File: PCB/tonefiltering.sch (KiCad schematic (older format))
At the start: 14 parts, among them U10 TS4990IST, U9 TS4990IST

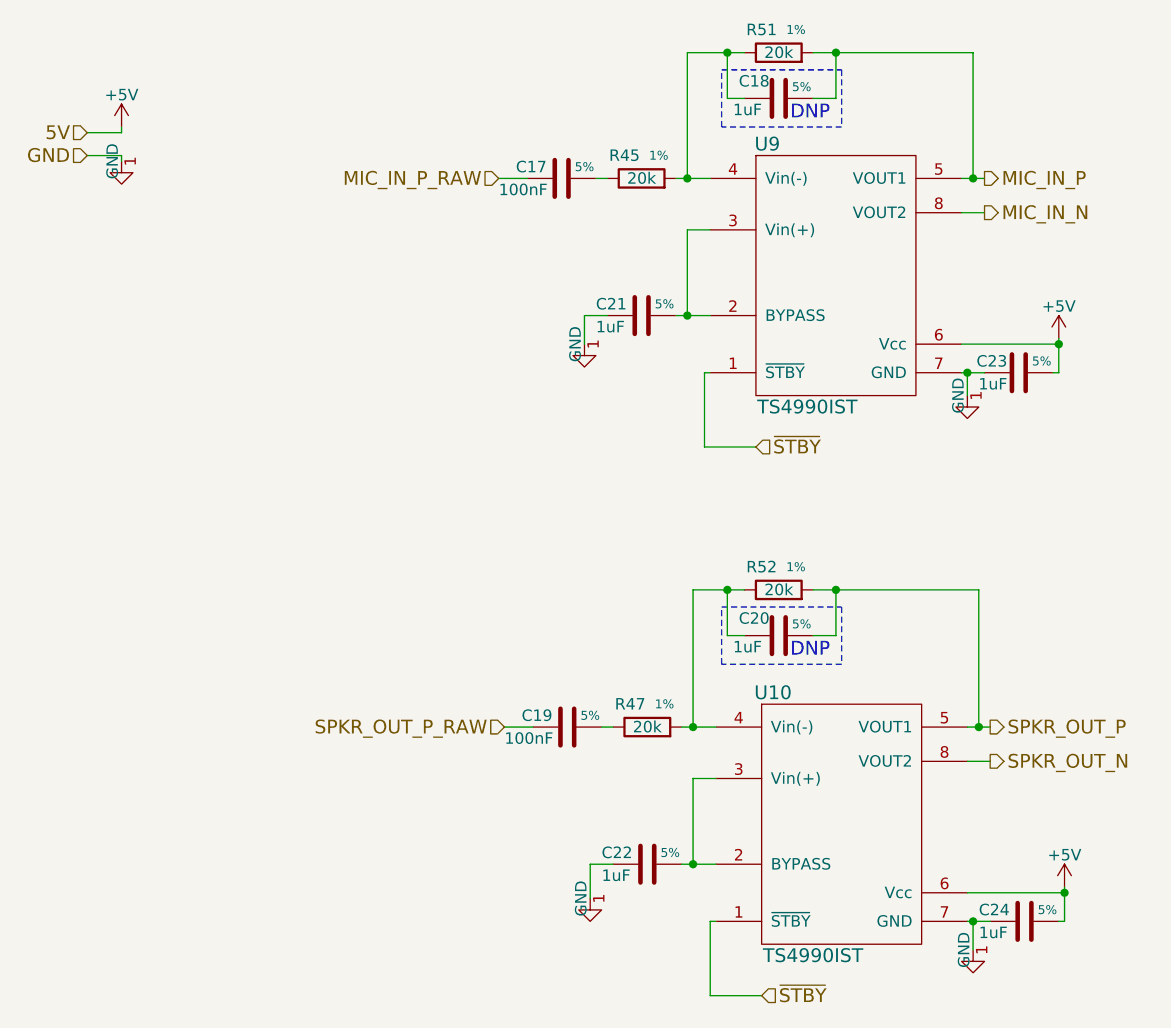
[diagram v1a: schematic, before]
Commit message: Added PCB layout
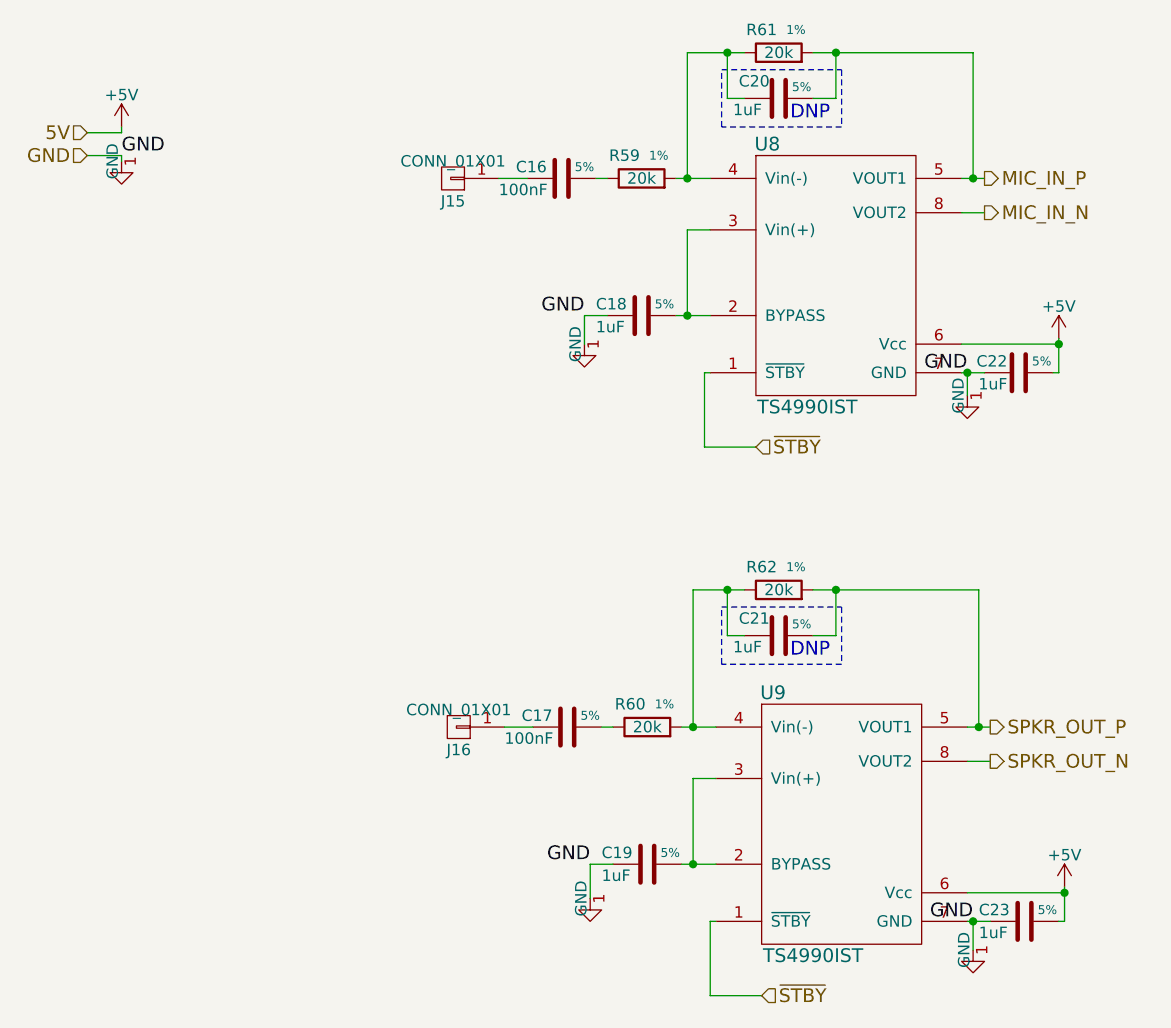
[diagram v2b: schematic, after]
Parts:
- added J15, J16: CONN_01X01, Pin_Headers:Pin_Header_Straight_1x01_Pitch2.54mm, symbol CONN_01X01
- C16: renamed from C17; footprint Footprints:1206 -> Capacitors_SMD:C_0603_HandSoldering
- C17: renamed from C19; footprint Footprints:1206 -> Capacitors_SMD:C_0603_HandSoldering
- C18: renamed from C21; footprint Footprints:1206 -> Capacitors_SMD:C_0603_HandSoldering
- C19: renamed from C22; footprint Footprints:1206 -> Capacitors_SMD:C_0603_HandSoldering
- C20: renamed from C18; footprint Footprints:1206 -> Capacitors_SMD:C_0603_HandSoldering
- C21: renamed from C20; footprint Footprints:1206 -> Capacitors_SMD:C_0603_HandSoldering
- C22: renamed from C23; footprint Footprints:1206 -> Capacitors_SMD:C_0603_HandSoldering
- C23: renamed from C24; footprint Footprints:1206 -> Capacitors_SMD:C_0603_HandSoldering
- R59: renamed from R45; footprint (none) -> Resistors_SMD:R_0603_HandSoldering
- R60: renamed from R47; footprint (none) -> Resistors_SMD:R_0603_HandSoldering
- R61: renamed from R51; footprint (none) -> Resistors_SMD:R_0603_HandSoldering
- R62: renamed from R52; footprint (none) -> Resistors_SMD:R_0603_HandSoldering
- U8: renamed from U9; footprint (none) -> Housings_SSOP:MSOP-8_3x3mm_Pitch0.65mm
- U9: renamed from U10; footprint (none) -> Housings_SSOP:MSOP-8_3x3mm_Pitch0.65mm
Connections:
- net GND: now also C18.2, C19.2, C22.1, C23.2, U8.7 (GND), U9.7 (GND)
- net MIC_IN_P_RAW: no longer names the net of C16.2
- net MIC_IN_P_RAW: now also J15.1 (P1)
- net SPKR_OUT_P_RAW: no longer names the net of C17.2
- net SPKR_OUT_P_RAW: now also J16.1 (P1)
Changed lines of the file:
@@
 $EndDescr
 $Comp
-L TS4990IST U9
+L TS4990IST U8
 U 1 1 5A23E919
 P 5200 2575
-F 0 "U9" H 5150 3025 60  0000 C CNN
+F 0 "U8" H 5150 3025 60  0000 C CNN
 F 1 "TS4990IST" H 5325 1875 60  0000 C CNN
-F 2 "" H 4500 3150 60  0001 C CNN
+F 2 "Housings_SSOP:MSOP-8_3x3mm_Pitch0.65mm" H 4500 3150 60  0001 C CNN
 F 3 "" H 4500 3150 60  0001 C CNN
 	1    5200 2575
@@
 $EndComp
 $Comp
-L C C17
+L C C16
 U 1 1 5A23E92A
 P 4250 2275
-F 0 "C17" V 4200 2075 50  0000 L CNN
+F 0 "C16" V 4200 2075 50  0000 L CNN
 F 1 "100nF" V 4300 2000 50  0000 L CNN
-F 2 "Footprints:1206" H 4288 2125 50  0001 C CNN
+F 2 "Capacitors_SMD:C_0603_HandSoldering" H 4288 2125 50  0001 C CNN
 F 3 "" H 4250 2275 50  0001 C CNN
 F 4 "5%" V 4200 2375 39  0000 C CNN "%"
@@
 	4400 2275 4450 2275
 $Comp
-L C C21
+L C C18
 U 1 1 5A23E93E
 P 4600 2875
-F 0 "C21" V 4550 2675 50  0000 L CNN
+F 0 "C18" V 4550 2675 50  0000 L CNN
 F 1 "1uF" V 4650 2675 50  0000 L CNN
-F 2 "Footprints:1206" H 4638 2725 50  0001 C CNN
+F 2 "Capacitors_SMD:C_0603_HandSoldering" H 4638 2725 50  0001 C CNN
 F 3 "" H 4600 2875 50  0001 C CNN
 F 4 "5%" V 4550 2975 39  0000 C CNN "%"
@@
 Connection ~ 4800 2875
 $Comp
-L C C23
+L C C22
 U 1 1 5A23E94C
 P 6250 3125
-F 0 "C23" V 6300 3175 50  0000 L CNN
+F 0 "C22" V 6300 3175 50  0000 L CNN
 F 1 "1uF" V 6200 3175 50  0000 L CNN
-F 2 "Footprints:1206" H 6288 2975 50  0001 C CNN
+F 2 "Capacitors_SMD:C_0603_HandSoldering" H 6288 2975 50  0001 C CNN
 F 3 "" H 6250 3125 50  0001 C CNN
 F 4 "5%" V 6300 3025 39  0000 C CNN "%"
@@
 	6000 2275 6100 2275
 $Comp
-L R R51
+L R R61
 U 1 1 5A23E96E
 P 5200 1725
-F 0 "R51" V 5300 1800 50  0000 C CNN
+F 0 "R61" V 5300 1800 50  0000 C CNN
 F 1 "20k" V 5200 1725 50  0000 C CNN
-F 2 "" V 5130 1725 50  0001 C CNN
+F 2 "Resistors_SMD:R_0603_HandSoldering" V 5130 1725 50  0001 C CNN
 F 3 "" H 5200 1725 50  0001 C CNN
 F 4 "1%" V 5300 1650 39  0000 C CNN "%"
@@
 Connection ~ 6050 2275
 $Comp
-L R R45
+L R R59
 U 1 1 5A23E97C
 P 4600 2275
-F 0 "R45" V 4700 2350 50  0000 C CNN
+F 0 "R59" V 4700 2350 50  0000 C CNN
 F 1 "20k" V 4600 2275 50  0000 C CNN
-F 2 "" V 4530 2275 50  0001 C CNN
+F 2 "Resistors_SMD:R_0603_HandSoldering" V 4530 2275 50  0001 C CNN
 F 3 "" H 4600 2275 50  0001 C CNN
 F 4 "1%" V 4700 2200 39  0000 C CNN "%"
@@
 $EndComp
 $Comp
-L TS4990IST U10
+L TS4990IST U9
 U 1 1 5A23E993
 P 5225 4975
-F 0 "U10" H 5175 5425 60  0000 C CNN
+F 0 "U9" H 5175 5425 60  0000 C CNN
 F 1 "TS4990IST" H 5350 4275 60  0000 C CNN
-F 2 "" H 4525 5550 60  0001 C CNN
+F 2 "Housings_SSOP:MSOP-8_3x3mm_Pitch0.65mm" H 4525 5550 60  0001 C CNN
 F 3 "" H 4525 5550 60  0001 C CNN
 	1    5225 4975
@@
 $EndComp
 $Comp
-L C C19
+L C C17
 U 1 1 5A23E9A4
 P 4275 4675
-F 0 "C19" V 4225 4475 50  0000 L CNN
+F 0 "C17" V 4225 4475 50  0000 L CNN
 F 1 "100nF" V 4325 4400 50  0000 L CNN
-F 2 "Footprints:1206" H 4313 4525 50  0001 C CNN
+F 2 "Capacitors_SMD:C_0603_HandSoldering" H 4313 4525 50  0001 C CNN
 F 3 "" H 4275 4675 50  0001 C CNN
 F 4 "5%" V 4225 4775 39  0000 C CNN "%"
@@
 	4425 4675 4475 4675
 $Comp
-L C C22
+L C C19
 U 1 1 5A23E9B8
 P 4625 5275
-F 0 "C22" V 4575 5075 50  0000 L CNN
+F 0 "C19" V 4575 5075 50  0000 L CNN
 F 1 "1uF" V 4675 5075 50  0000 L CNN
-F 2 "Footprints:1206" H 4663 5125 50  0001 C CNN
+F 2 "Capacitors_SMD:C_0603_HandSoldering" H 4663 5125 50  0001 C CNN
 F 3 "" H 4625 5275 50  0001 C CNN
 F 4 "5%" V 4575 5375 39  0000 C CNN "%"
@@
 Connection ~ 4825 5275
 $Comp
-L C C24
+L C C23
 U 1 1 5A23E9C6
 P 6275 5525
-F 0 "C24" V 6225 5325 50  0000 L CNN
+F 0 "C23" V 6225 5325 50  0000 L CNN
 F 1 "1uF" V 6325 5325 50  0000 L CNN
-F 2 "Footprints:1206" H 6313 5375 50  0001 C CNN
+F 2 "Capacitors_SMD:C_0603_HandSoldering" H 6313 5375 50  0001 C CNN
 F 3 "" H 6275 5525 50  0001 C CNN
 F 4 "5%" V 6225 5625 39  0000 C CNN "%"
@@
 	6025 4675 6125 4675
 $Comp
-L R R52
+L R R62
 U 1 1 5A23E9E5
 P 5200 4075
-F 0 "R52" V 5300 4150 50  0000 C CNN
+F 0 "R62" V 5300 4150 50  0000 C CNN
 F 1 "20k" V 5200 4075 50  0000 C CNN
-F 2 "" V 5130 4075 50  0001 C CNN
+F 2 "Resistors_SMD:R_0603_HandSoldering" V 5130 4075 50  0001 C CNN
 F 3 "" H 5200 4075 50  0001 C CNN
 F 4 "1%" V 5300 4000 39  0000 C CNN "%"
@@
 Connection ~ 6075 4675
 $Comp
-L R R47
+L R R60
 U 1 1 5A23E9F3
 P 4625 4675
-F 0 "R47" V 4725 4750 50  0000 C CNN
+F 0 "R60" V 4725 4750 50  0000 C CNN
 F 1 "20k" V 4625 4675 50  0000 C CNN
-F 2 "" V 4555 4675 50  0001 C CNN
+F 2 "Resistors_SMD:R_0603_HandSoldering" V 4555 4675 50  0001 C CNN
 F 3 "" H 4625 4675 50  0001 C CNN
 F 4 "1%" V 4725 4600 39  0000 C CNN "%"
@@
 	0    -1   -1   0
 $EndComp
-Text HLabel 3975 2275 0    60   Input ~ 0
-MIC_IN_P_RAW
 Text HLabel 6100 2275 2    60   Output ~ 0
 MIC_IN_P
@@
 Text HLabel 6125 4825 2    60   Output ~ 0
 SPKR_OUT_N
-Text HLabel 4000 4675 0    60   Input ~ 0
-SPKR_OUT_P_RAW
 Text HLabel 2175 2175 0    60   Input ~ 0
 GND
 $Comp
-L GND-RESCUE-Tardis #PWR083
+L GND-RESCUE-Tardis #PWR081
 U 1 1 5A35F2E4
 P 2325 2200
-AR Path="/5A35F2E4" Ref="#PWR083"  Part="1"
-AR Path="/5A2392E1/5A35F2E4" Ref="#PWR86"  Part="1"
-F 0 "#PWR86" H 2325 1950 50  0001 C CNN
+F 0 "#PWR081" H 2325 1950 50  0001 C CNN
 F 1 "GND" H 2325 2050 50  0001 C CNN
 F 2 "" H 2325 2200 50  0001 C CNN
@@
 	2325 2175 2325 2200
 $Comp
-L +5V #PWR85
+L +5V #PWR082
 U 1 1 5A35F2EC
 P 2325 2050
-F 0 "#PWR85" H 2325 1900 50  0001 C CNN
+F 0 "#PWR082" H 2325 1900 50  0001 C CNN
 F 1 "+5V" H 2325 2190 50  0000 C CNN
 F 2 "" H 2325 2050 50  0001 C CNN
@@
 	2325 2075 2325 2050
 $Comp
-L +5V #PWR91
+L +5V #PWR083
 U 1 1 5A35F319
 P 6425 2975
-F 0 "#PWR91" H 6425 2825 50  0001 C CNN
+F 0 "#PWR083" H 6425 2825 50  0001 C CNN
 F 1 "+5V" H 6425 3115 50  0000 C CNN
 F 2 "" H 6425 2975 50  0001 C CNN
@@
 $EndComp
 $Comp
-L GND-RESCUE-Tardis #PWR086
+L GND-RESCUE-Tardis #PWR084
 U 1 1 5A35F35A
 P 4350 3000
-AR Path="/5A35F35A" Ref="#PWR086"  Part="1"
-AR Path="/5A2392E1/5A35F35A" Ref="#PWR87"  Part="1"
-F 0 "#PWR87" H 4350 2750 50  0001 C CNN
+F 0 "#PWR084" H 4350 2750 50  0001 C CNN
 F 1 "GND" H 4350 2850 50  0001 C CNN
 F 2 "" H 4350 3000 50  0001 C CNN
@@
 $EndComp
 $Comp
-L GND-RESCUE-Tardis #PWR087
+L GND-RESCUE-Tardis #PWR085
 U 1 1 5A35F491
 P 6025 3225
-AR Path="/5A35F491" Ref="#PWR087"  Part="1"
-AR Path="/5A2392E1/5A35F491" Ref="#PWR89"  Part="1"
-F 0 "#PWR89" H 6025 2975 50  0001 C CNN
+F 0 "#PWR085" H 6025 2975 50  0001 C CNN
 F 1 "GND" H 6025 3075 50  0001 C CNN
 F 2 "" H 6025 3225 50  0001 C CNN
@@
 $EndComp
 $Comp
-L +5V #PWR92
+L +5V #PWR086
 U 1 1 5A35F52A
 P 6450 5375
-F 0 "#PWR92" H 6450 5225 50  0001 C CNN
+F 0 "#PWR086" H 6450 5225 50  0001 C CNN
 F 1 "+5V" H 6450 5515 50  0000 C CNN
 F 2 "" H 6450 5375 50  0001 C CNN
@@
 $EndComp
 $Comp
-L GND-RESCUE-Tardis #PWR089
+L GND-RESCUE-Tardis #PWR087
 U 1 1 5A35F5FB
 P 4375 5425
-AR Path="/5A35F5FB" Ref="#PWR089"  Part="1"
-AR Path="/5A2392E1/5A35F5FB" Ref="#PWR88"  Part="1"
-F 0 "#PWR88" H 4375 5175 50  0001 C CNN
+F 0 "#PWR087" H 4375 5175 50  0001 C CNN
 F 1 "GND" H 4375 5275 50  0001 C CNN
 F 2 "" H 4375 5425 50  0001 C CNN
@@
 $EndComp
 $Comp
-L GND-RESCUE-Tardis #PWR090
+L GND-RESCUE-Tardis #PWR088
 U 1 1 5A35F714
 P 6050 5650
-AR Path="/5A35F714" Ref="#PWR090"  Part="1"
-AR Path="/5A2392E1/5A35F714" Ref="#PWR90"  Part="1"
-F 0 "#PWR90" H 6050 5400 50  0001 C CNN
+F 0 "#PWR088" H 6050 5400 50  0001 C CNN
 F 1 "GND" H 6050 5500 50  0001 C CNN
 F 2 "" H 6050 5650 50  0001 C CNN
@@
 	4925 4900 4825 4900
 $Comp
-L C C18
+L C C20
 U 1 1 5A24E9E5
 P 5200 1925
-F 0 "C18" V 5125 1750 50  0000 L CNN
+F 0 "C20" V 5125 1750 50  0000 L CNN
 F 1 "1uF" V 5250 1725 50  0000 L CNN
-F 2 "Footprints:1206" H 5238 1775 50  0001 C CNN
+F 2 "Capacitors_SMD:C_0603_HandSoldering" H 5238 1775 50  0001 C CNN
 F 3 "" H 5200 1925 50  0001 C CNN
 F 4 "5%" V 5150 2025 39  0000 C CNN "%"
@@
 	4900 5850 5125 5850
 $Comp
-L C C20
+L C C21
 U 1 1 5A25010F
 P 5200 4275
-F 0 "C20" V 5125 4100 50  0000 L CNN
+F 0 "C21" V 5125 4100 50  0000 L CNN
 F 1 "1uF" V 5250 4075 50  0000 L CNN
-F 2 "Footprints:1206" H 5238 4125 50  0001 C CNN
+F 2 "Capacitors_SMD:C_0603_HandSoldering" H 5238 4125 50  0001 C CNN
 F 3 "" H 5200 4275 50  0001 C CNN
 F 4 "5%" V 5150 4375 39  0000 C CNN "%"
@@
 	5350 4075 6075 4075
 Connection ~ 5450 4075
+Text Label 2325 2175 0    60   ~ 0
+GND
+Text Label 4350 2875 2    60   ~ 0
+GND
+Text Label 6025 3125 2    60   ~ 0
+GND
+Text Label 6050 5525 2    60   ~ 0
+GND
+Text Label 4375 5275 2    60   ~ 0
+GND
+$Comp
+L CONN_01X01 J16
+U 1 1 5A55D9A8
+P 3800 4675
+F 0 "J16" H 3800 4775 50  0000 C CNN
+F 1 "CONN_01X01" H 3800 4600 50  0000 C CNN
+F 2 "Pin_Headers:Pin_Header_Straight_1x01_Pitch2.54mm" H 3800 4675 50  0001 C CNN
+F 3 "" H 3800 4675 50  0001 C CNN
+	1    3800 4675
+	-1   0    0    1
+$EndComp
+$Comp
+L CONN_01X01 J15
+U 1 1 5A55DA84
+P 3775 2275
+F 0 "J15" H 3775 2375 50  0000 C CNN
+F 1 "CONN_01X01" H 3775 2200 50  0000 C CNN
+F 2 "Pin_Headers:Pin_Header_Straight_1x01_Pitch2.54mm" H 3775 2275 50  0001 C CNN
+F 3 "" H 3775 2275 50  0001 C CNN
+	1    3775 2275
+	-1   0    0    1
+$EndComp
 $EndSCHEMATC
